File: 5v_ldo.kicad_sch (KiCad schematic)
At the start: 0 parts

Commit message: Removed TR switch sheet and brought it into the RX path sheet
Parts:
- added C1501: 100nF 25V, BR_Passives:C_0201_0603Metric-minimized, symbol BR_Capacitors_0201:C_0201_100nF_25V_X7R_10%
- added C1502: 330nF 16V, BR_Passives:C_0402_1005Metric-minimized, symbol BR_Capacitors_0402:C_0402_330nF_16V_X7R_10%
- added U1501: ~, BR_SOT:SOT-23, symbol BR_IC_Regulators:MG78L05T3
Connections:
- new net GND: C1501.2, C1502.2, U1501.3 (GND)
- new net VIN: C1502.1, U1501.2 (VI)
- new net VOUT: C1501.1, U1501.1 (VO)

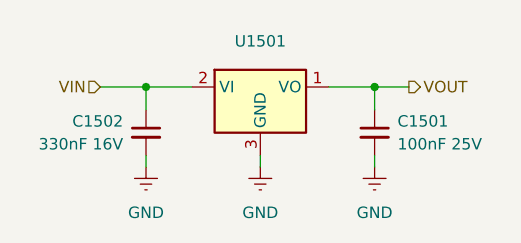
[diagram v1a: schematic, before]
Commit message: completed feedback from review + reannotated sheets
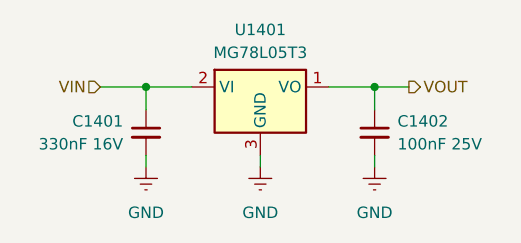
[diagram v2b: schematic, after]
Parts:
- U1401: renamed from U1501; value ~ -> MG78L05T3
- renumbered C1502 to C1401, C1501 to C1402
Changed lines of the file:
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@@
 		(dnp no)
 		(fields_autoplaced yes)
-		(property "Reference" "#PWR01501"
+		(property "Reference" "#PWR01402"
 			(at 104.14 74.93 0)
 			(effects
@@
 			(project ""
 				(path "/2a5ce3ef-537a-4122-a1be-ef76186bc0d7/774f2c6c-c15c-4713-acf0-4edb2ec6be20/d89bd557-813e-4016-ac7f-80185426a1bc"
-					(reference "#PWR01501")
+					(reference "#PWR01402")
 					(unit 1)
 				)
@@
 		(on_board yes)
 		(dnp no)
-		(property "Reference" "C1502"
+		(property "Reference" "C1401"
 			(at 88.9 63.5062 0)
 			(effects
@@
 			(project ""
 				(path "/2a5ce3ef-537a-4122-a1be-ef76186bc0d7/774f2c6c-c15c-4713-acf0-4edb2ec6be20/d89bd557-813e-4016-ac7f-80185426a1bc"
-					(reference "C1502")
+					(reference "C1401")
 					(unit 1)
 				)
@@
 		(dnp no)
 		(fields_autoplaced yes)
-		(property "Reference" "U1501"
-			(at 104.14 54.61 0)
-			(effects
-				(font
-					(size 1.27 1.27)
-				)
-			)
-		)
-		(property "Value" "~"
+		(property "Reference" "U1401"
+			(at 104.14 53.34 0)
+			(effects
+				(font
+					(size 1.27 1.27)
+				)
+			)
+		)
+		(property "Value" "MG78L05T3"
 			(at 104.14 55.88 0)
 			(effects
@@
 			(project ""
 				(path "/2a5ce3ef-537a-4122-a1be-ef76186bc0d7/774f2c6c-c15c-4713-acf0-4edb2ec6be20/d89bd557-813e-4016-ac7f-80185426a1bc"
-					(reference "U1501")
+					(reference "U1401")
 					(unit 1)
 				)
@@
 		(dnp no)
 		(fields_autoplaced yes)
-		(property "Reference" "#PWR01502"
+		(property "Reference" "#PWR01401"
 			(at 91.44 74.93 0)
 			(effects
@@
 			(project "SonarDevBoard"
 				(path "/2a5ce3ef-537a-4122-a1be-ef76186bc0d7/774f2c6c-c15c-4713-acf0-4edb2ec6be20/d89bd557-813e-4016-ac7f-80185426a1bc"
-					(reference "#PWR01502")
+					(reference "#PWR01401")
 					(unit 1)
 				)
@@
 		(dnp no)
 		(fields_autoplaced yes)
-		(property "Reference" "#PWR01503"
+		(property "Reference" "#PWR01403"
 			(at 116.84 74.93 0)
 			(effects
@@
 			(project "SonarDevBoard"
 				(path "/2a5ce3ef-537a-4122-a1be-ef76186bc0d7/774f2c6c-c15c-4713-acf0-4edb2ec6be20/d89bd557-813e-4016-ac7f-80185426a1bc"
-					(reference "#PWR01503")
+					(reference "#PWR01403")
 					(unit 1)
 				)
@@
 		(dnp no)
 		(fields_autoplaced yes)
-		(property "Reference" "C1501"
+		(property "Reference" "C1402"
 			(at 119.38 63.5062 0)
 			(effects
@@
 			(project ""
 				(path "/2a5ce3ef-537a-4122-a1be-ef76186bc0d7/774f2c6c-c15c-4713-acf0-4edb2ec6be20/d89bd557-813e-4016-ac7f-80185426a1bc"
-					(reference "C1501")
+					(reference "C1402")
 					(unit 1)
 				)
